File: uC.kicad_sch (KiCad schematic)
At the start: 20 parts, among them J3 Conn_01x04, J4 Conn_01x05, J5 5023860270, U3 STM32G431KBT6, Y1 ECS-2520MV-xxx-xx

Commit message: did some stuff yesterday i dont remember
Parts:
- added J6: Conn_01x04, Connector_PinSocket_2.54mm:PinSocket_1x04_P2.54mm_Vertical, symbol Connector_Generic:Conn_01x04
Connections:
- new net CAN/CANH: J6.1 (Pin_1), J6.2 (Pin_2)
- new net CAN/CANL: J6.3 (Pin_3), J6.4 (Pin_4)
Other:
- added sheet CAN (CAN.kicad_sch)
- moved on the sheet: C25, J3, J4, R12, R13, R16

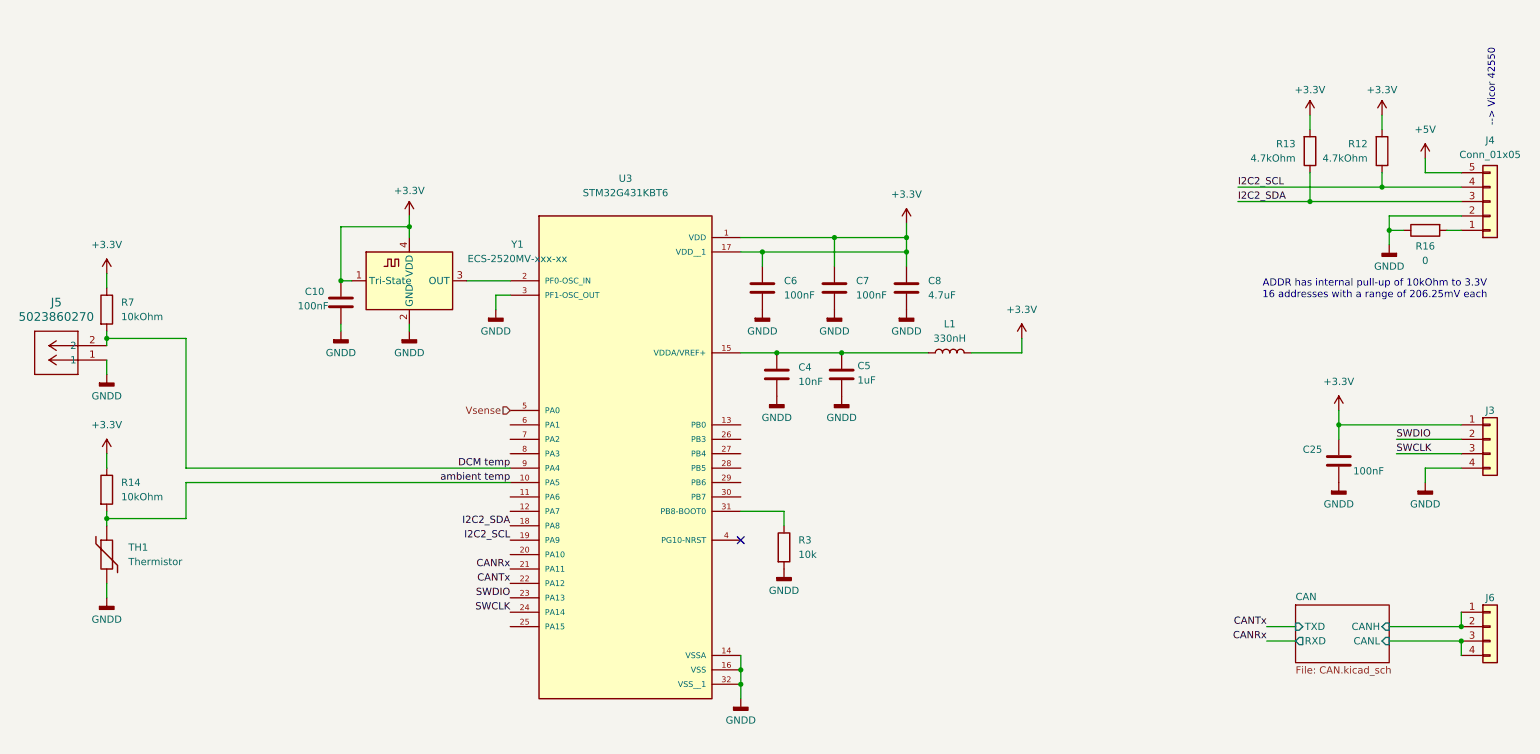
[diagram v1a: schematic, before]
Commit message: Made trim circuit
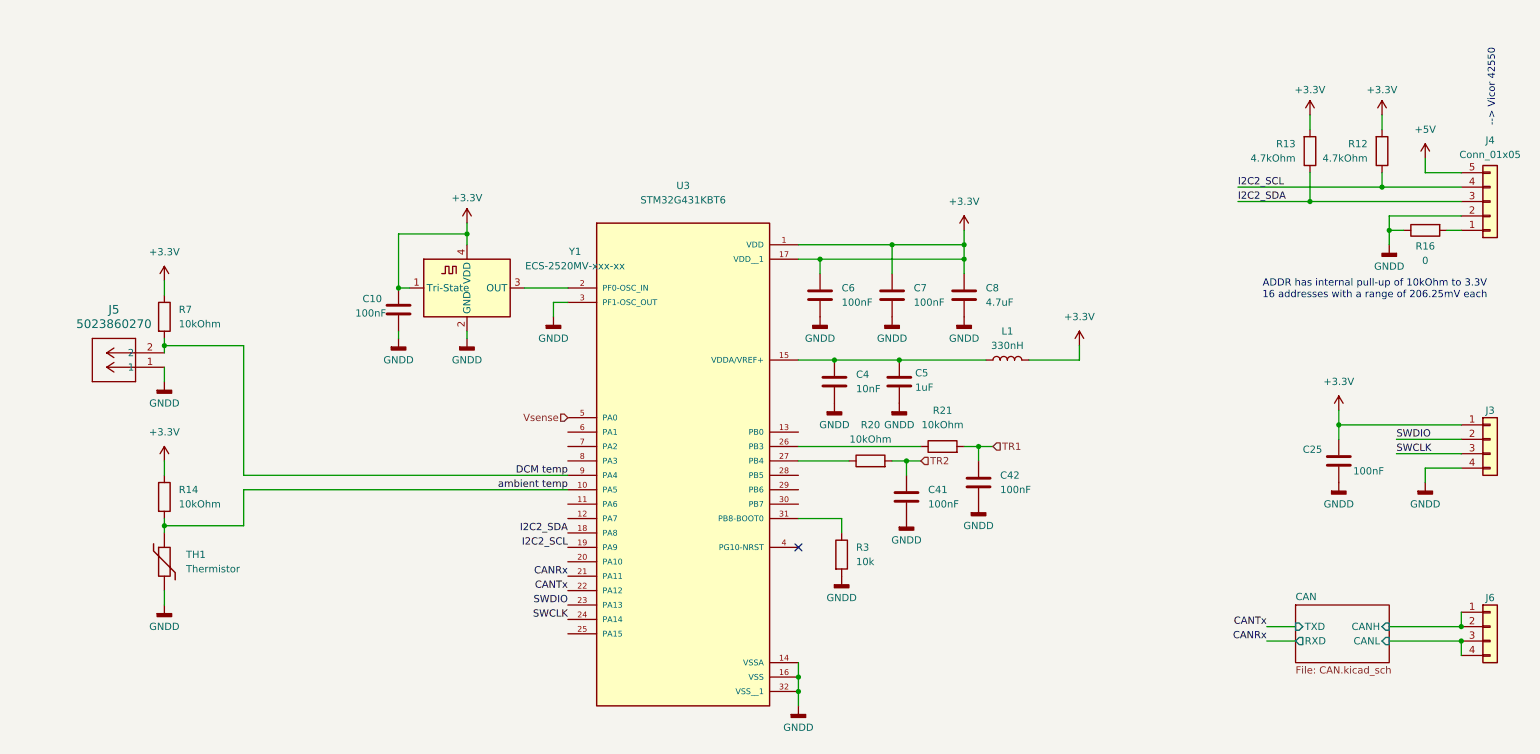
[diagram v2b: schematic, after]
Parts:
- added C41, C42: 100nF, symbol Device:C
- added R20, R21: 10kOhm, symbol Device:R
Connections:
- net GNDD: now also C41.1, C42.1
- net at U3.26 (PB3): now also R21.1
- net at U3.27 (PB4): now also R20.1
- new net TR1: C42.2, R21.2
- new net TR2: C41.2, R20.2
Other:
- moved on the sheet: C10, C4, C5, C6, C7, C8, J5, L1, R14, R3, R7, TH1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

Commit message: added shunts
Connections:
- net CurrSense1: now reaches U3.6 (PA1)
- net CurrSense2: now reaches U3.7 (PA2)

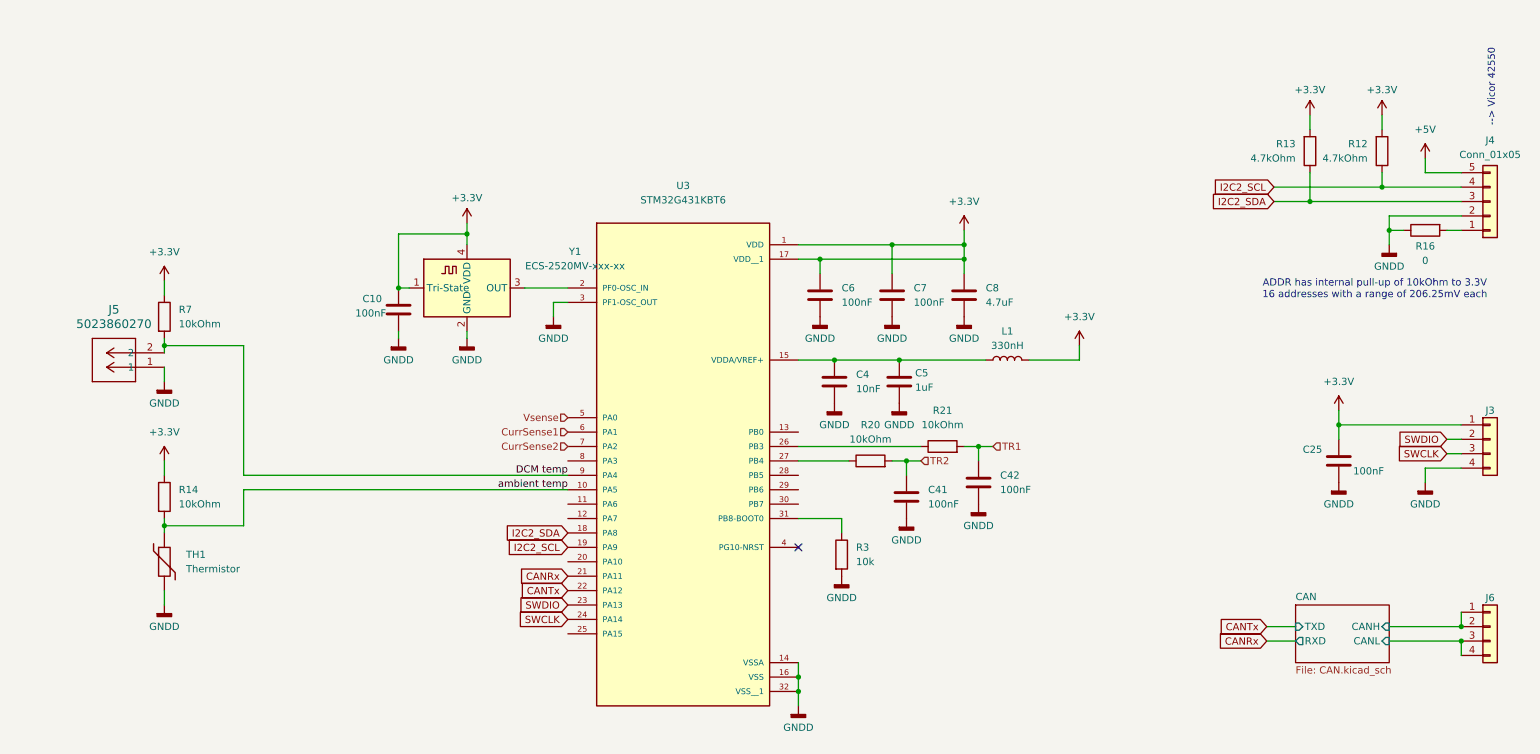
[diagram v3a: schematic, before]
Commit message: assigned footprints, some minor schematic stuff, started layout
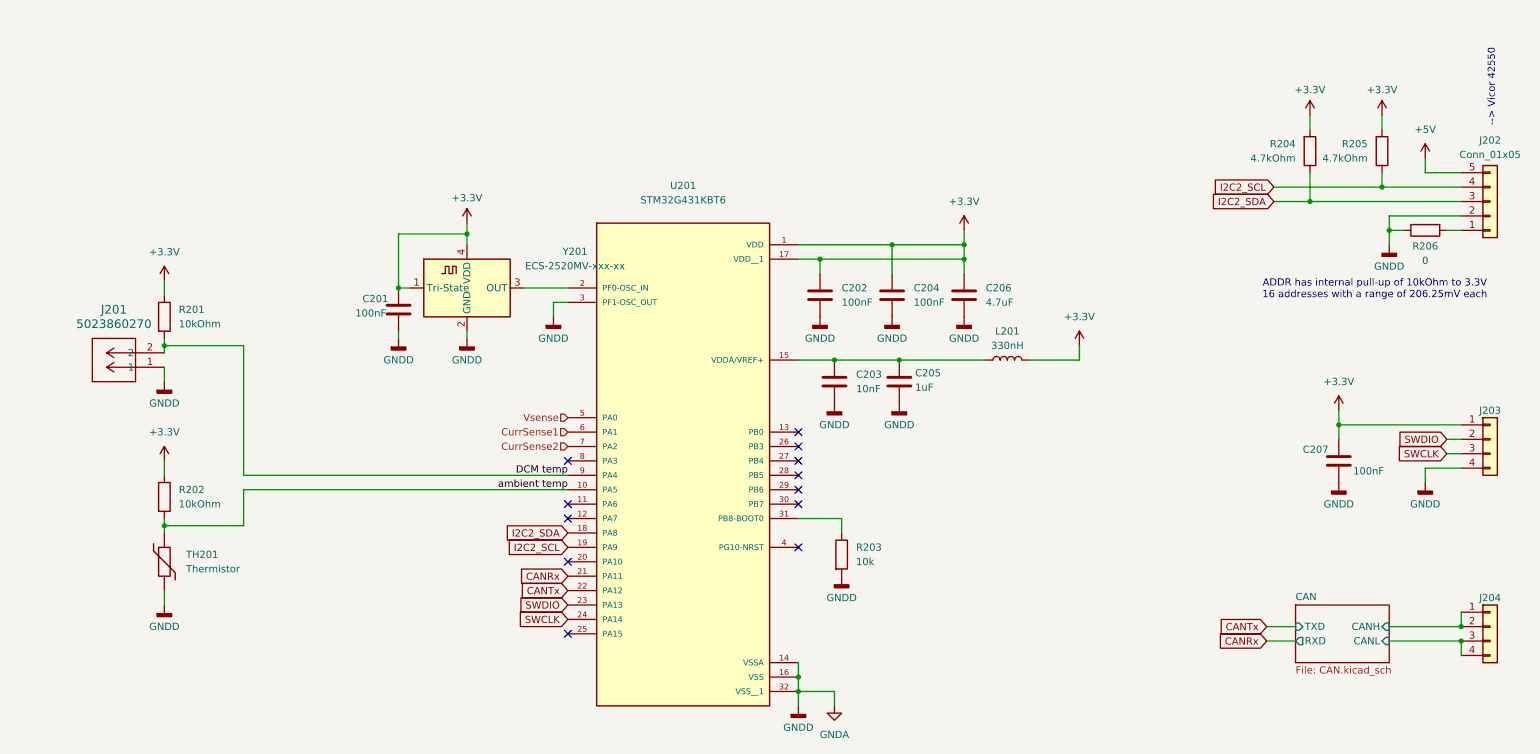
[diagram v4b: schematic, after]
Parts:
- removed C41, C42: 100nF, symbol Device:C
- removed R20, R21: 10kOhm, symbol Device:R
- C201: renamed from C10; footprint (none) -> Capacitor_SMD:C_0805_2012Metric
- C202: renamed from C6; footprint (none) -> Capacitor_SMD:C_0805_2012Metric
- C203: renamed from C4; footprint (none) -> Capacitor_SMD:C_0805_2012Metric
- C204: renamed from C7; footprint (none) -> Capacitor_SMD:C_0603_1608Metric
- C205: renamed from C5; footprint (none) -> Capacitor_SMD:C_0603_1608Metric
- C206: renamed from C8; footprint (none) -> Capacitor_SMD:C_0603_1608Metric
- J201: renamed from J5; footprint CONN_502386-02xx_MOL -> footprints:CONN_502386-02xx_MOL
- J202: renamed from J4; footprint (none) -> Connector_PinHeader_2.54mm:PinHeader_2x05_P2.54mm_Vertical
- J204: renamed from J6; footprint Connector_PinSocket_2.54mm:PinSocket_1x04_P2.54mm_Vertical -> Connector_PinHeader_2.54mm:PinHeader_2x04_P2.54mm_Vertical
- L201: renamed from L1; footprint (none) -> Inductor_SMD:L_0805_2012Metric
- R201: renamed from R7; footprint (none) -> Resistor_SMD:R_0603_1608Metric
- R202: renamed from R14; footprint (none) -> Resistor_SMD:R_0603_1608Metric
- R203: renamed from R3; footprint (none) -> Resistor_SMD:R_0603_1608Metric
- R204: renamed from R13; footprint (none) -> Resistor_SMD:R_0603_1608Metric
- R205: renamed from R12; footprint (none) -> Resistor_SMD:R_0603_1608Metric
- R206: renamed from R16; footprint (none) -> Resistor_SMD:R_0603_1608Metric
- TH201: renamed from TH1; footprint (none) -> Resistor_SMD:R_0805_2012Metric
- U201: renamed from U3; footprint STM32G431KBT6:QFP80P900X900X160-32N -> Package_QFP:LQFP-32_7x7mm_P0.8mm
- renumbered C25 to C207, J3 to J203, Y1 to Y201
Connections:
- net GNDD renamed GNDA
- no-connect marks 1 -> 12

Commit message: progress on layout in general, minor tweaks to schemas
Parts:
- added C208: 4.7uF, Capacitor_SMD:C_0603_1608Metric, symbol Device:C
- C201, C202, C203: footprint Capacitor_SMD:C_0805_2012Metric -> Capacitor_SMD:C_0603_1608Metric
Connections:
- net +3.3V: now also J203.4 (Pin_4), C208.1; no longer J203.1 (Pin_1)
- net GNDA: now also J203.1 (Pin_1), C208.2; no longer J203.4 (Pin_4)
- net SWCLK: now also J203.2 (Pin_2); no longer J203.3 (Pin_3)
- net SWDIO: now also J203.3 (Pin_3); no longer J203.2 (Pin_2)
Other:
- moved on the sheet: L201

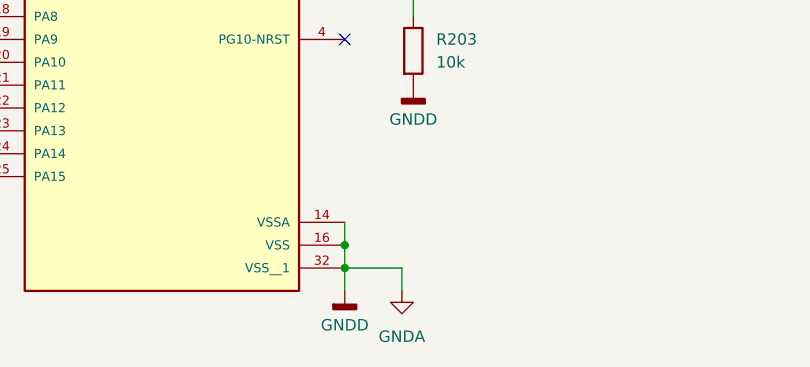
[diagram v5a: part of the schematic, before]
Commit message: made heatsink holes
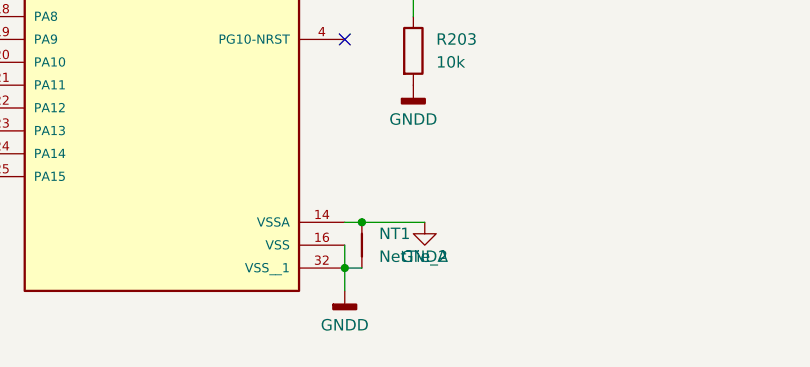
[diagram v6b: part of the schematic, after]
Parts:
- added NT1: NetTie_2, NetTie:NetTie-2_SMD_Pad2.0mm, symbol Device:NetTie_2
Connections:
- net GNDA: now also NT1.2; no longer C201.2, C202.2, C203.2, C204.2, C205.2, C206.2, C207.2, C208.2, J201.1, J202.2 (Pin_2), J203.1 (Pin_1), R203.2, R206.1, TH201.2, U201.16 (VSS), U201.3 (PF1-OSC_OUT), U201.32 (VSS__1), Y201.2 (GND)
- new net GNDD: C201.2, C202.2, C203.2, C204.2, C205.2, C206.2, C207.2, C208.2, J201.1, J202.2 (Pin_2), J203.1 (Pin_1), NT1.1, R203.2, R206.1, TH201.2, U201.16 (VSS), U201.3 (PF1-OSC_OUT), U201.32 (VSS__1), Y201.2 (GND)
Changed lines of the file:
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@@
 	)
 	(junction
+		(at 156.21 142.24)
+		(diameter 0)
+		(color 0 0 0 0)
+	)
+	(junction
 		(at 273.05 133.35)
 		(diameter 0)
@@
 	)
 	(junction
-		(at 156.21 139.7)
+		(at 158.115 137.16)
 		(diameter 0)
 		(color 0 0 0 0)
@@
 	)
 	(junction
-		(at 156.21 142.24)
-		(diameter 0)
-		(color 0 0 0 0)
-	)
-	(junction
 		(at 162.56 83.82)
 		(diameter 0)
@@
 	(wire
 		(pts
-			(xy 162.56 142.24) (xy 156.21 142.24)
-		)
-		(stroke
-			(width 0)
-			(type default)
-		)
-	)
-	(wire
-		(pts
 			(xy 160.02 66.04) (xy 160.02 68.58)
 		)
@@
 	(wire
 		(pts
-			(xy 238.76 133.35) (xy 243.84 133.35)
+			(xy 156.21 139.7) (xy 156.21 142.24)
 		)
 		(stroke
@@
 	(wire
 		(pts
-			(xy 156.21 142.24) (xy 156.21 144.78)
+			(xy 238.76 133.35) (xy 243.84 133.35)
 		)
 		(stroke
@@
 	(wire
 		(pts
-			(xy 162.56 144.78) (xy 162.56 142.24)
-		)
-		(stroke
-			(width 0)
-			(type default)
-		)
-	)
-	(wire
-		(pts
 			(xy 259.08 40.64) (xy 259.08 43.18)
 		)
@@
 	(wire
 		(pts
-			(xy 156.21 137.16) (xy 156.21 139.7)
-		)
-		(stroke
-			(width 0)
-			(type default)
-		)
-	)
-	(wire
-		(pts
 			(xy 251.46 95.25) (xy 273.05 95.25)
 		)
@@
 	(wire
 		(pts
+			(xy 156.21 142.24) (xy 158.115 142.24)
+		)
+		(stroke
+			(width 0)
+			(type default)
+		)
+	)
+	(wire
+		(pts
 			(xy 156.21 83.82) (xy 162.56 83.82)
 		)
@@
 	(wire
 		(pts
-			(xy 156.21 139.7) (xy 156.21 142.24)
+			(xy 156.21 142.24) (xy 156.21 144.78)
+		)
+		(stroke
+			(width 0)
+			(type default)
+		)
+	)
+	(wire
+		(pts
+			(xy 158.115 137.16) (xy 165.1 137.16)
 		)
 		(stroke
@@
 	(wire
 		(pts
+			(xy 156.21 137.16) (xy 158.115 137.16)
+		)
+		(stroke
+			(width 0)
+			(type default)
+		)
+	)
+	(wire
+		(pts
 			(xy 172.72 63.5) (xy 198.12 63.5)
 		)
@@
 	)
 	(symbol
+		(lib_id "Device:NetTie_2")
+		(at 158.115 139.7 90)
+		(unit 1)
+		(body_style 1)
+		(exclude_from_sim no)
+		(in_bom no)
+		(on_board yes)
+		(in_pos_files yes)
+		(dnp no)
+		(fields_autoplaced yes)
+		(property "Reference" "NT1"
+			(at 160.02 138.4299 90)
+			(show_name no)
+			(do_not_autoplace no)
+			(effects
+				(font
+					(size 1.27 1.27)
+				)
+				(justify right)
+			)
+		)
+		(property "Value" "NetTie_2"
+			(at 160.02 140.9699 90)
+			(show_name no)
+			(do_not_autoplace no)
+			(effects
+				(font
+					(size 1.27 1.27)
+				)
+				(justify right)
+			)
+		)
+		(property "Footprint" "NetTie:NetTie-2_SMD_Pad2.0mm"
+			(at 158.115 139.7 0)
+			(hide yes)
+			(show_name no)
+			(do_not_autoplace no)
+			(effects
+				(font
+					(size 1.27 1.27)
+				)
+			)
+		)
+		(property "Datasheet" ""
+			(at 158.115 139.7 0)
+			(hide yes)
+			(show_name no)
+			(do_not_autoplace no)
+			(effects
+				(font
+					(size 1.27 1.27)
+				)
+			)
+		)
+		(property "Description" "Net tie, 2 pins"
+			(at 158.115 139.7 0)
+			(hide yes)
+			(show_name no)
+			(do_not_autoplace no)
+			(effects
+				(font
+					(size 1.27 1.27)
+				)
+			)
+		)
+		(pin "2"
+		)
+		(pin "1"
+		)
+		(instances
+			(project "LV_DCDC"
+				(path "/ccad4640-78c7-423b-83df-3ec0b90aa2b3/f9342e9a-2c81-4a9f-bedf-76ac3e437a63"
+					(reference "NT1")
+					(unit 1)
+				)
+			)
+		)
+	)
+	(symbol
 		(lib_id "Connector_Generic:Conn_01x04")
 		(at 278.13 100.33 0)
@@
 	(symbol
 		(lib_id "power:GNDA")
-		(at 162.56 144.78 0)
+		(at 165.1 137.16 0)
 		(unit 1)
 		(body_style 1)
@@
 		(in_pos_files yes)
 		(dnp no)
-		(fields_autoplaced yes)
 		(property "Reference" "#PWR0212"
-			(at 162.56 151.13 0)
+			(at 165.1 143.51 0)
 			(hide yes)
 			(show_name no)
@@
 		)
 		(property "Value" "GNDA"
-			(at 162.56 149.86 0)
+			(at 165.1 140.97 0)
 			(show_name no)
 			(do_not_autoplace no)
@@
 		)
 		(property "Footprint" ""
-			(at 162.56 144.78 0)
+			(at 165.1 137.16 0)
 			(hide yes)
 			(show_name no)
@@
 		)
 		(property "Datasheet" ""
-			(at 162.56 144.78 0)
+			(at 165.1 137.16 0)
 			(hide yes)
 			(show_name no)
@@
 		)
 		(property "Description" "Power symbol creates a global label with name \"GNDA\" , analog ground"
-			(at 162.56 144.78 0)
+			(at 165.1 137.16 0)
 			(hide yes)
 			(show_name no)
